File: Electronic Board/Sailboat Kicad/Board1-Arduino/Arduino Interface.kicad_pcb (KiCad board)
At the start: 2 copper layers, 69.9 x 101 mm, 58 parts, among them J1 Conn_01x02, J10 Conn_01x02, J11 Conn_01x03_Male, J12 Conn_01x03_Male, J13 Conn_01x03_Male, J14 Conn_01x03_Male, J15 Conn_01x04, J16 Conn_01x04, J17 Conn_01x04, J18 Conn_01x04, J19 Conn_01x03, J2 Conn_01x08, J20 Conn_01x03, J21 Conn_01x02, J22 Conn_01x02, J23 Conn_01x06, J24 Conn_01x03, J25 Conn_01x06, J26 Conn_02x02_Odd_Even, J3 Conn_01x08, J31 Conn_01x04, J32 Conn_01x04, J34 Conn_01x02, J35 Conn_01x02, J36 Conn_01x02, J37 Conn_01x02, J4 Conn_01x08, J5 Conn_02x18_Odd_Even, J6 Conn_01x08, J7 Conn_01x08, J8 Conn_01x08, J9 Conn_01x02, U1 L7805, U2 L7805, U3 L7805

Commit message: Minor changes and recompiled gerber, pdf and 3D
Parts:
- C1, C2, C3, C4, D1, D2, D3, D4, D5, J36, J37, L1, L2, R1, R2, R3, R4, R5: moved to B.Cu
- turned J36 to 270 degrees
- turned J37 to 270 degrees

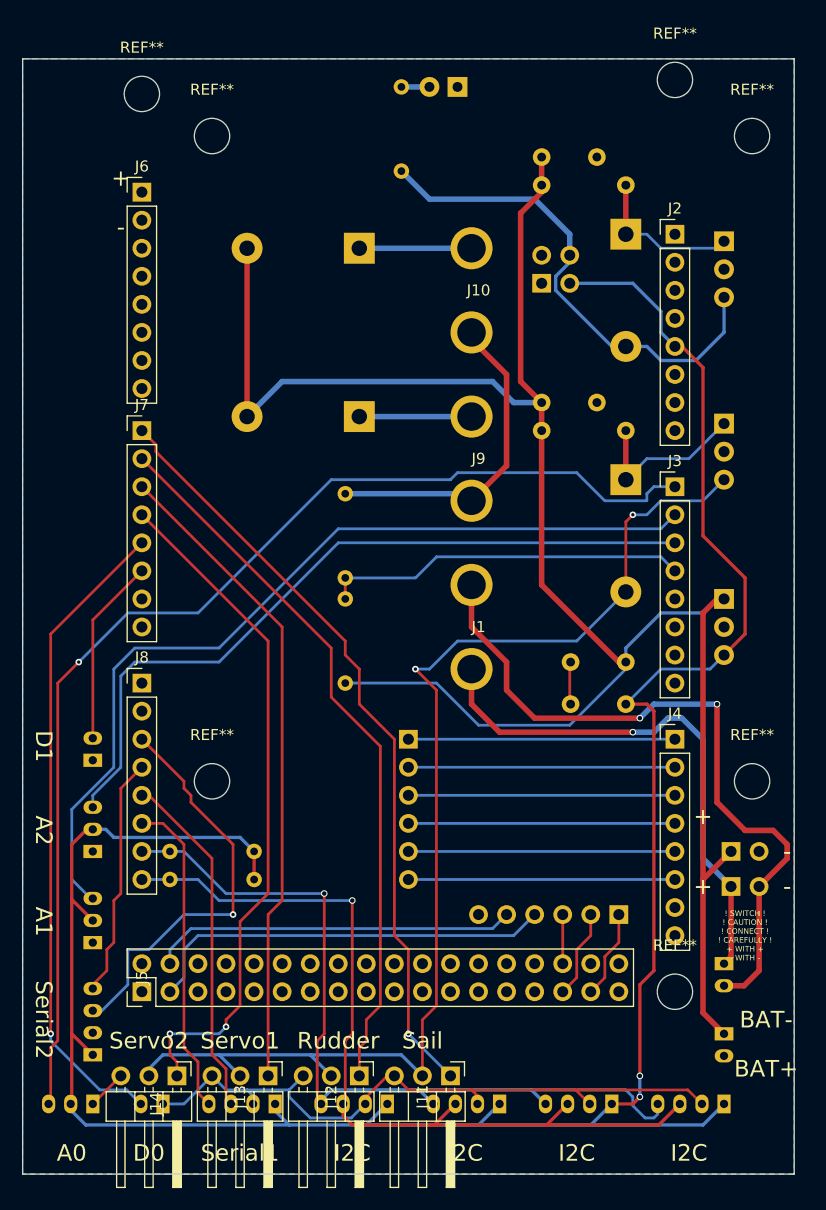
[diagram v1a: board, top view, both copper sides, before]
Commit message: Changed size to be smaller than 100mm
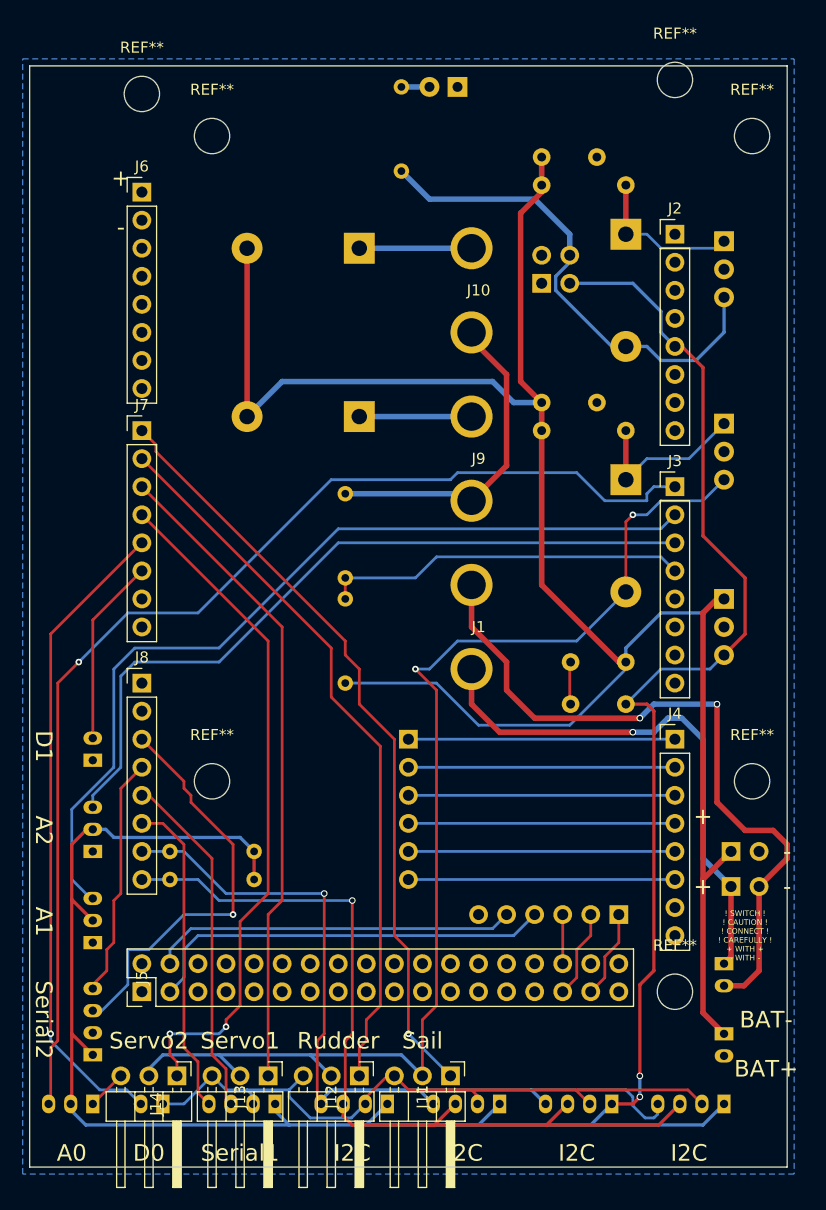
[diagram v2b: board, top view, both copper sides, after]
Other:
- board size 69.9 x 101 mm -> 68.6 x 99.7 mm
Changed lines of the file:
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@@
     (pcbplotparams
       (layerselection 0x010f0_80000001)
-      (usegerberextensions false)
+      (usegerberextensions true)
       (excludeedgelayer true)
       (linewidth 0.100000)
@@
       (padsonsilk false)
       (subtractmaskfromsilk false)
-      (outputformat 4)
+      (outputformat 1)
       (mirror false)
       (drillshape 0)
@@
     (pad 1 np_thru_hole circle (at 0 0) (size 3.2 3.2) (drill 3.2) (layers *.Cu *.Mask))
   )
+  (gr_line (start 118.745 153.035) (end 118.745 53.34) (angle 90) (layer Edge.Cuts) (width 0.1))
+  (gr_line (start 187.325 153.035) (end 118.745 153.035) (angle 90) (layer Edge.Cuts) (width 0.1))
+  (gr_line (start 187.325 53.34) (end 187.325 153.035) (angle 90) (layer Edge.Cuts) (width 0.1))
+  (gr_line (start 118.745 53.34) (end 187.325 53.34) (angle 90) (layer Edge.Cuts) (width 0.1))
   (gr_text Sensors-5V (at 186.055 104.775 90) (layer B.SilkS)
     (effects (font (size 1.5 1.5) (thickness 0.3)) (justify mirror))
@@
     (effects (font (size 1.5 1.5) (thickness 0.3)))
   )
-  (gr_line (start 118.11 52.705) (end 118.11 153.67) (angle 90) (layer Edge.Cuts) (width 0.1))
-  (gr_line (start 187.96 52.705) (end 187.96 153.67) (angle 90) (layer Edge.Cuts) (width 0.1))
   (gr_line (start 187.96 121.92) (end 187.96 36.195) (angle 90) (layer Eco1.User) (width 0.2))
-  (gr_line (start 118.11 52.705) (end 187.96 52.705) (angle 90) (layer Edge.Cuts) (width 0.1))
-  (gr_line (start 187.96 153.67) (end 118.11 153.67) (angle 90) (layer Edge.Cuts) (width 0.1))
   (gr_text - (at 187.325 124.46) (layer F.SilkS)
     (effects (font (size 1.5 1.5) (thickness 0.3)))

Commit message: New board bug fix
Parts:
- moved J37 0.64 mm to (182.2, 125.1)
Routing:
- net BAT+: track 180.8 -> 180.3 mm
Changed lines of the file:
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@@
     (thickness 1.6)
     (drawings 66)
-    (tracks 378)
+    (tracks 380)
     (zones 0)
     (modules 58)
@@
       (drillshape 0)
       (scaleselection 1)
-      (outputdirectory PDF/))
+      (outputdirectory Gerber/))
   )
   (net 0 "")
@@
   )
   (module Pin_Headers:Pin_Header_Straight_1x02_Pitch2.54mm (layer B.Cu)
-    (at 182.245 124.46 270)
+    (at 182.245 125.095 270)
     (descr "Through hole straight pin header, 1x02, 2.54mm pitch, single row")
     (tags "Through hole pin header THT 1x02 2.54mm single row")
@@
     (effects (font (size 1.5 1.5) (thickness 0.3)))
   )
-  (gr_text BAT- (at 185.42 139.7) (layer F.SilkS)
+  (gr_text BAT- (at 185.42 133.985) (layer F.SilkS)
     (effects (font (size 1.5 1.5) (thickness 0.3)))
   )
-  (gr_text BAT+ (at 185.42 144.145) (layer F.SilkS)
+  (gr_text BAT+ (at 185.42 137.16) (layer F.SilkS)
     (effects (font (size 1.5 1.5) (thickness 0.3)))
   )
@@
   (gr_line (start 131.445 36.195) (end 131.445 121.92) (angle 90) (layer Eco1.User) (width 0.2))
   (gr_line (start 187.96 36.195) (end 131.445 36.195) (angle 90) (layer Eco1.User) (width 0.2))
+  (segment (start 179.705 126.365) (end 180.975 125.095) (width 0.5) (layer F.Cu) (net 1))
+  (segment (start 180.975 125.095) (end 182.245 125.095) (width 0.5) (layer F.Cu) (net 1))
   (segment (start 165.1 83.82) (end 162.56 83.82) (width 0.5) (layer B.Cu) (net 1) (status 10))
   (segment (start 141.605 81.915) (end 138.43 85.09) (width 0.5) (layer B.Cu) (net 1) (status 20))
@@
   (segment (start 179.705 102.87) (end 175.895 102.87) (width 0.3) (layer B.Cu) (net 1))
   (segment (start 180.975 101.6) (end 179.705 102.87) (width 0.5) (layer F.Cu) (net 1) (status 10))
-  (segment (start 179.705 102.87) (end 179.705 127) (width 0.5) (layer F.Cu) (net 1))
-  (segment (start 182.245 124.46) (end 179.705 127) (width 0.5) (layer F.Cu) (net 1) (status 10))
+  (segment (start 179.705 102.87) (end 179.705 126.365) (width 0.5) (layer F.Cu) (net 1))
+  (segment (start 179.705 126.365) (end 179.705 127) (width 0.5) (layer F.Cu) (net 1))
   (segment (start 179.705 139.065) (end 181.61 140.97) (width 0.5) (layer F.Cu) (net 1) (status 20))
   (segment (start 179.705 127) (end 179.705 139.065) (width 0.5) (layer F.Cu) (net 1))

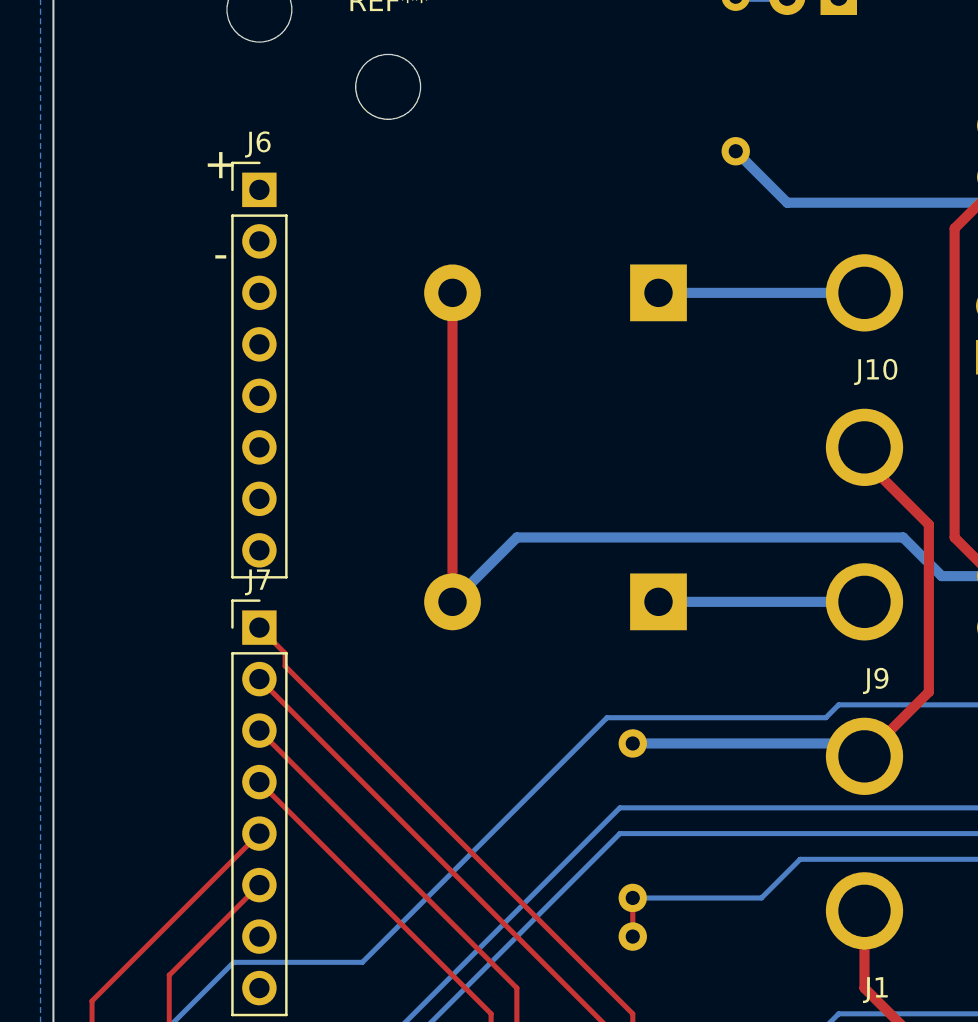
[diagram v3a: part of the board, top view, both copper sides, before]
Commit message: added decoupler capacitor for voltage measurements and added connectors to arduino
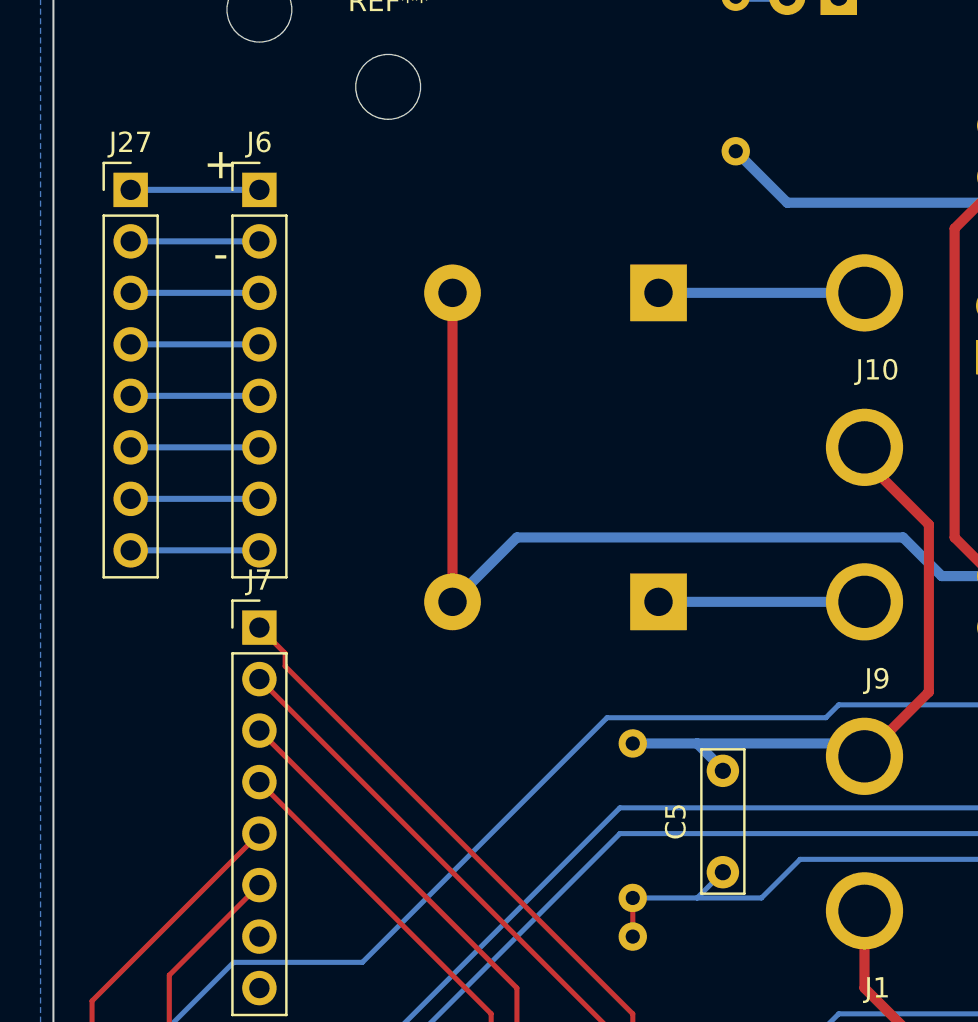
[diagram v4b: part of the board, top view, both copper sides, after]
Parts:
- added C5: 1uF, Capacitors_THT:C_Rect_L7.0mm_W2.0mm_P5.00mm, F.Cu at (151.8, 98.4)
- added J27: Conn_01x08, Pin_Headers:Pin_Header_Straight_1x08_Pitch2.54mm, F.Cu at (122.6, 64.8)
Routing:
- net GND: track 98.1 -> 106.3 mm
- net /ArduinoMega/AREF: track 0.00 -> 6.35 mm
- net /ArduinoMega/9: track 0.00 -> 6.35 mm
- net /ArduinoMega/8: track 0.00 -> 6.35 mm
- net /ArduinoMega/13: track 0.00 -> 6.35 mm
- net /ArduinoMega/12: track 0.00 -> 6.35 mm
- net /ArduinoMega/11: track 0.00 -> 6.35 mm
- net /ArduinoMega/10: track 0.00 -> 6.35 mm
- net /ArduinoMega/A3: track 33.1 -> 34.9 mm
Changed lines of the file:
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@@
-(kicad_pcb (version 4) (host pcbnew 4.0.7)
+(kicad_pcb (version 4) (host pcbnew 4.0.7-e2-6376~58~ubuntu16.04.1)
   (general
-    (links 113)
+    (links 123)
     (no_connects 0)
     (area 116.235 36.094999 193.707143 156.007858)
     (thickness 1.6)
     (drawings 66)
-    (tracks 380)
+    (tracks 393)
     (zones 0)
-    (modules 58)
+    (modules 60)
     (nets 92)
   )
@@
     (pcbplotparams
       (layerselection 0x010f0_80000001)
-      (usegerberextensions true)
+      (usegerberextensions false)
       (excludeedgelayer true)
       (linewidth 0.100000)
@@
       (padsonsilk false)
       (subtractmaskfromsilk false)
-      (outputformat 1)
+      (outputformat 4)
       (mirror false)
       (drillshape 0)
       (scaleselection 1)
-      (outputdirectory Gerber/))
+      (outputdirectory PDF/))
   )
   (net 0 "")
@@
     (pad 1 np_thru_hole circle (at 0 0) (size 3.2 3.2) (drill 3.2) (layers *.Cu *.Mask))
   )
+  (module Capacitors_THT:C_Rect_L7.0mm_W2.0mm_P5.00mm (layer F.Cu)
+    (at 151.765 98.425 90)
+    (descr "C, Rect series, Radial, pin pitch=5.00mm, , length*width=7*2mm^2, Capacitor")
+    (tags "C Rect series Radial pin pitch 5.00mm  length 7mm width 2mm Capacitor")
+    (fp_text reference C5 (at 2.5 -2.31 90) (layer F.SilkS)
+      (effects (font (size 1 1) (thickness 0.15)))
+    )
+    (fp_text value 1uF (at 2.5 2.31 90) (layer F.Fab)
+      (effects (font (size 1 1) (thickness 0.15)))
+    )
+    (fp_line (start -1 -1) (end -1 1) (layer F.Fab) (width 0.1))
+    (fp_line (start -1 1) (end 6 1) (layer F.Fab) (width 0.1))
+    (fp_line (start 6 1) (end 6 -1) (layer F.Fab) (width 0.1))
+    (fp_line (start 6 -1) (end -1 -1) (layer F.Fab) (width 0.1))
+    (fp_line (start -1.06 -1.06) (end 6.06 -1.06) (layer F.SilkS) (width 0.12))
+    (fp_line (start -1.06 1.06) (end 6.06 1.06) (layer F.SilkS) (width 0.12))
+    (fp_line (start -1.06 -1.06) (end -1.06 1.06) (layer F.SilkS) (width 0.12))
+    (fp_line (start 6.06 -1.06) (end 6.06 1.06) (layer F.SilkS) (width 0.12))
+    (fp_line (start -1.35 -1.35) (end -1.35 1.35) (layer F.CrtYd) (width 0.05))
+    (fp_line (start -1.35 1.35) (end 6.35 1.35) (layer F.CrtYd) (width 0.05))
+    (fp_line (start 6.35 1.35) (end 6.35 -1.35) (layer F.CrtYd) (width 0.05))
+    (fp_line (start 6.35 -1.35) (end -1.35 -1.35) (layer F.CrtYd) (width 0.05))
+    (fp_text user %R (at 2.5 0 90) (layer F.Fab)
+      (effects (font (size 1 1) (thickness 0.15)))
+    )
+    (pad 1 thru_hole circle (at 0 0 90) (size 1.6 1.6) (drill 0.8) (layers *.Cu *.Mask)
+      (net 12 /ArduinoMega/A3))
+    (pad 2 thru_hole circle (at 5 0 90) (size 1.6 1.6) (drill 0.8) (layers *.Cu *.Mask)
+      (net 2 GND))
+    (model ${KISYS3DMOD}/Capacitors_THT.3dshapes/C_Rect_L7.0mm_W2.0mm_P5.00mm.wrl
+      (at (xyz 0 0 0))
+      (scale (xyz 1 1 1))
+      (rotate (xyz 0 0 0))
+    )
+  )
+  (module Pin_Headers:Pin_Header_Straight_1x08_Pitch2.54mm (layer F.Cu)
+    (at 122.555 64.77)
+    (descr "Through hole straight pin header, 1x08, 2.54mm pitch, single row")
+    (tags "Through hole pin header THT 1x08 2.54mm single row")
+    (fp_text reference J27 (at 0 -2.33) (layer F.SilkS)
+      (effects (font (size 1 1) (thickness 0.15)))
+    )
+    (fp_text value Conn_01x08 (at 0 20.11) (layer F.Fab)
+      (effects (font (size 1 1) (thickness 0.15)))
+    )
+    (fp_line (start -0.635 -1.27) (end 1.27 -1.27) (layer F.Fab) (width 0.1))
+    (fp_line (start 1.27 -1.27) (end 1.27 19.05) (layer F.Fab) (width 0.1))
+    (fp_line (start 1.27 19.05) (end -1.27 19.05) (layer F.Fab) (width 0.1))
+    (fp_line (start -1.27 19.05) (end -1.27 -0.635) (layer F.Fab) (width 0.1))
+    (fp_line (start -1.27 -0.635) (end -0.635 -1.27) (layer F.Fab) (width 0.1))
+    (fp_line (start -1.33 19.11) (end 1.33 19.11) (layer F.SilkS) (width 0.12))
+    (fp_line (start -1.33 1.27) (end -1.33 19.11) (layer F.SilkS) (width 0.12))
+    (fp_line (start 1.33 1.27) (end 1.33 19.11) (layer F.SilkS) (width 0.12))
+    (fp_line (start -1.33 1.27) (end 1.33 1.27) (layer F.SilkS) (width 0.12))
+    (fp_line (start -1.33 0) (end -1.33 -1.33) (layer F.SilkS) (width 0.12))
+    (fp_line (start -1.33 -1.33) (end 0 -1.33) (layer F.SilkS) (width 0.12))
+    (fp_line (start -1.8 -1.8) (end -1.8 19.55) (layer F.CrtYd) (width 0.05))
+    (fp_line (start -1.8 19.55) (end 1.8 19.55) (layer F.CrtYd) (width 0.05))
+    (fp_line (start 1.8 19.55) (end 1.8 -1.8) (layer F.CrtYd) (width 0.05))
+    (fp_line (start 1.8 -1.8) (end -1.8 -1.8) (layer F.CrtYd) (width 0.05))
+    (fp_text user %R (at 0 8.89 90) (layer F.Fab)
+      (effects (font (size 1 1) (thickness 0.15)))
+    )
+    (pad 1 thru_hole rect (at 0 0) (size 1.7 1.7) (drill 1) (layers *.Cu *.Mask)
+      (net 51 /ArduinoMega/AREF))
+    (pad 2 thru_hole oval (at 0 2.54) (size 1.7 1.7) (drill 1) (layers *.Cu *.Mask)
+      (net 2 GND))
+    (pad 3 thru_hole oval (at 0 5.08) (size 1.7 1.7) (drill 1) (layers *.Cu *.Mask)
+      (net 83 /ArduinoMega/13))
+    (pad 4 thru_hole oval (at 0 7.62) (size 1.7 1.7) (drill 1) (layers *.Cu *.Mask)
+      (net 84 /ArduinoMega/12))
+    (pad 5 thru_hole oval (at 0 10.16) (size 1.7 1.7) (drill 1) (layers *.Cu *.Mask)
+      (net 85 /ArduinoMega/11))
+    (pad 6 thru_hole oval (at 0 12.7) (size 1.7 1.7) (drill 1) (layers *.Cu *.Mask)
+      (net 86 /ArduinoMega/10))
+    (pad 7 thru_hole oval (at 0 15.24) (size 1.7 1.7) (drill 1) (layers *.Cu *.Mask)
+      (net 87 /ArduinoMega/9))
+    (pad 8 thru_hole oval (at 0 17.78) (size 1.7 1.7) (drill 1) (layers *.Cu *.Mask)
+      (net 88 /ArduinoMega/8))
+    (model ${KISYS3DMOD}/Pin_Headers.3dshapes/Pin_Header_Straight_1x08_Pitch2.54mm.wrl
+      (at (xyz 0 0 0))
+      (scale (xyz 1 1 1))
+      (rotate (xyz 0 0 0))
+    )
+  )
   (gr_line (start 118.745 153.035) (end 118.745 53.34) (angle 90) (layer Edge.Cuts) (width 0.1))
   (gr_line (start 187.325 153.035) (end 118.745 153.035) (angle 90) (layer Edge.Cuts) (width 0.1))
@@
   (segment (start 172.72 107.95) (end 172.72 107.315) (width 0.25) (layer B.Cu) (net 1) (status 30))
   (segment (start 155.575 109.22) (end 159.385 113.03) (width 0.25) (layer B.Cu) (net 1))
-  (segment (start 147.32 92.075) (end 158.115 92.075) (width 0.5) (layer B.Cu) (net 2) (status 30))
+  (segment (start 122.555 67.31) (end 128.905 67.31) (width 0.3) (layer B.Cu) (net 2))
+  (segment (start 151.765 93.425) (end 151.765 93.345) (width 0.5) (layer B.Cu) (net 2))
+  (segment (start 151.765 93.345) (end 150.495 92.075) (width 0.5) (layer B.Cu) (net 2))
+  (segment (start 147.32 92.075) (end 150.495 92.075) (width 0.5) (layer B.Cu) (net 2) (status 30))
+  (segment (start 150.495 92.075) (end 158.115 92.075) (width 0.5) (layer B.Cu) (net 2) (status 30))
   (segment (start 158.115 92.075) (end 158.75 92.71) (width 0.5) (layer B.Cu) (net 2) (status 30))
   (segment (start 158.75 78.105) (end 161.925 81.28) (width 0.5) (layer F.Cu) (net 2) (status 10))
@@
   (segment (start 127 108.585) (end 128.27 107.315) (width 0.25) (layer B.Cu) (net 11))
   (segment (start 146.685 96.52) (end 177.165 96.52) (width 0.25) (layer B.Cu) (net 11) (status 20))
+  (segment (start 151.765 98.425) (end 150.495 99.695) (width 0.25) (layer B.Cu) (net 12))
   (segment (start 147.32 101.6) (end 147.32 99.695) (width 0.25) (layer F.Cu) (net 12) (status 30))
-  (segment (start 147.32 99.695) (end 153.67 99.695) (width 0.25) (layer B.Cu) (net 12) (status 10))
+  (segment (start 147.32 99.695) (end 150.495 99.695) (width 0.25) (layer B.Cu) (net 12) (status 10))
+  (segment (start 150.495 99.695) (end 153.67 99.695) (width 0.25) (layer B.Cu) (net 12) (status 10))
   (segment (start 175.895 97.79) (end 177.165 99.06) (width 0.25) (layer B.Cu) (net 12) (status 20))
   (segment (start 155.575 97.79) (end 175.895 97.79) (width 0.25) (layer B.Cu) (net 12))
@@
   (segment (start 170.815 133.985) (end 172.085 132.715) (width 0.25) (layer F.Cu) (net 49))
   (segment (start 170.815 135.89) (end 170.815 133.985) (width 0.25) (layer F.Cu) (net 49))
+  (segment (start 128.905 64.77) (end 122.555 64.77) (width 0.3) (layer B.Cu) (net 51))
   (segment (start 177.165 127) (end 153.035 127) (width 0.25) (layer B.Cu) (net 52) (status 30))
   (segment (start 153.035 124.46) (end 177.165 124.46) (width 0.25) (layer B.Cu) (net 53) (status 30))
@@
   (segment (start 172.72 64.135) (end 172.72 68.58) (width 0.5) (layer F.Cu) (net 82) (status 30))
   (segment (start 180.975 69.85) (end 181.61 69.215) (width 0.25) (layer B.Cu) (net 82) (status 30))
+  (segment (start 128.905 69.85) (end 122.555 69.85) (width 0.3) (layer B.Cu) (net 83))
+  (segment (start 122.555 72.39) (end 128.905 72.39) (width 0.3) (layer B.Cu) (net 84))
+  (segment (start 128.905 74.93) (end 122.555 74.93) (width 0.3) (layer B.Cu) (net 85))
+  (segment (start 122.555 77.47) (end 128.905 77.47) (width 0.3) (layer B.Cu) (net 86))
+  (segment (start 128.905 80.01) (end 122.555 80.01) (width 0.3) (layer B.Cu) (net 87))
+  (segment (start 122.555 82.55) (end 128.905 82.55) (width 0.3) (layer B.Cu) (net 88))
   (segment (start 148.59 85.09) (end 158.75 85.09) (width 0.5) (layer B.Cu) (net 89) (status 30))
   (segment (start 148.59 69.85) (end 158.75 69.85) (width 0.5) (layer B.Cu) (net 90) (status 30))
